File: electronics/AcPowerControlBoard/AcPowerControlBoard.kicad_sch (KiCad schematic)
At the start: 1 part

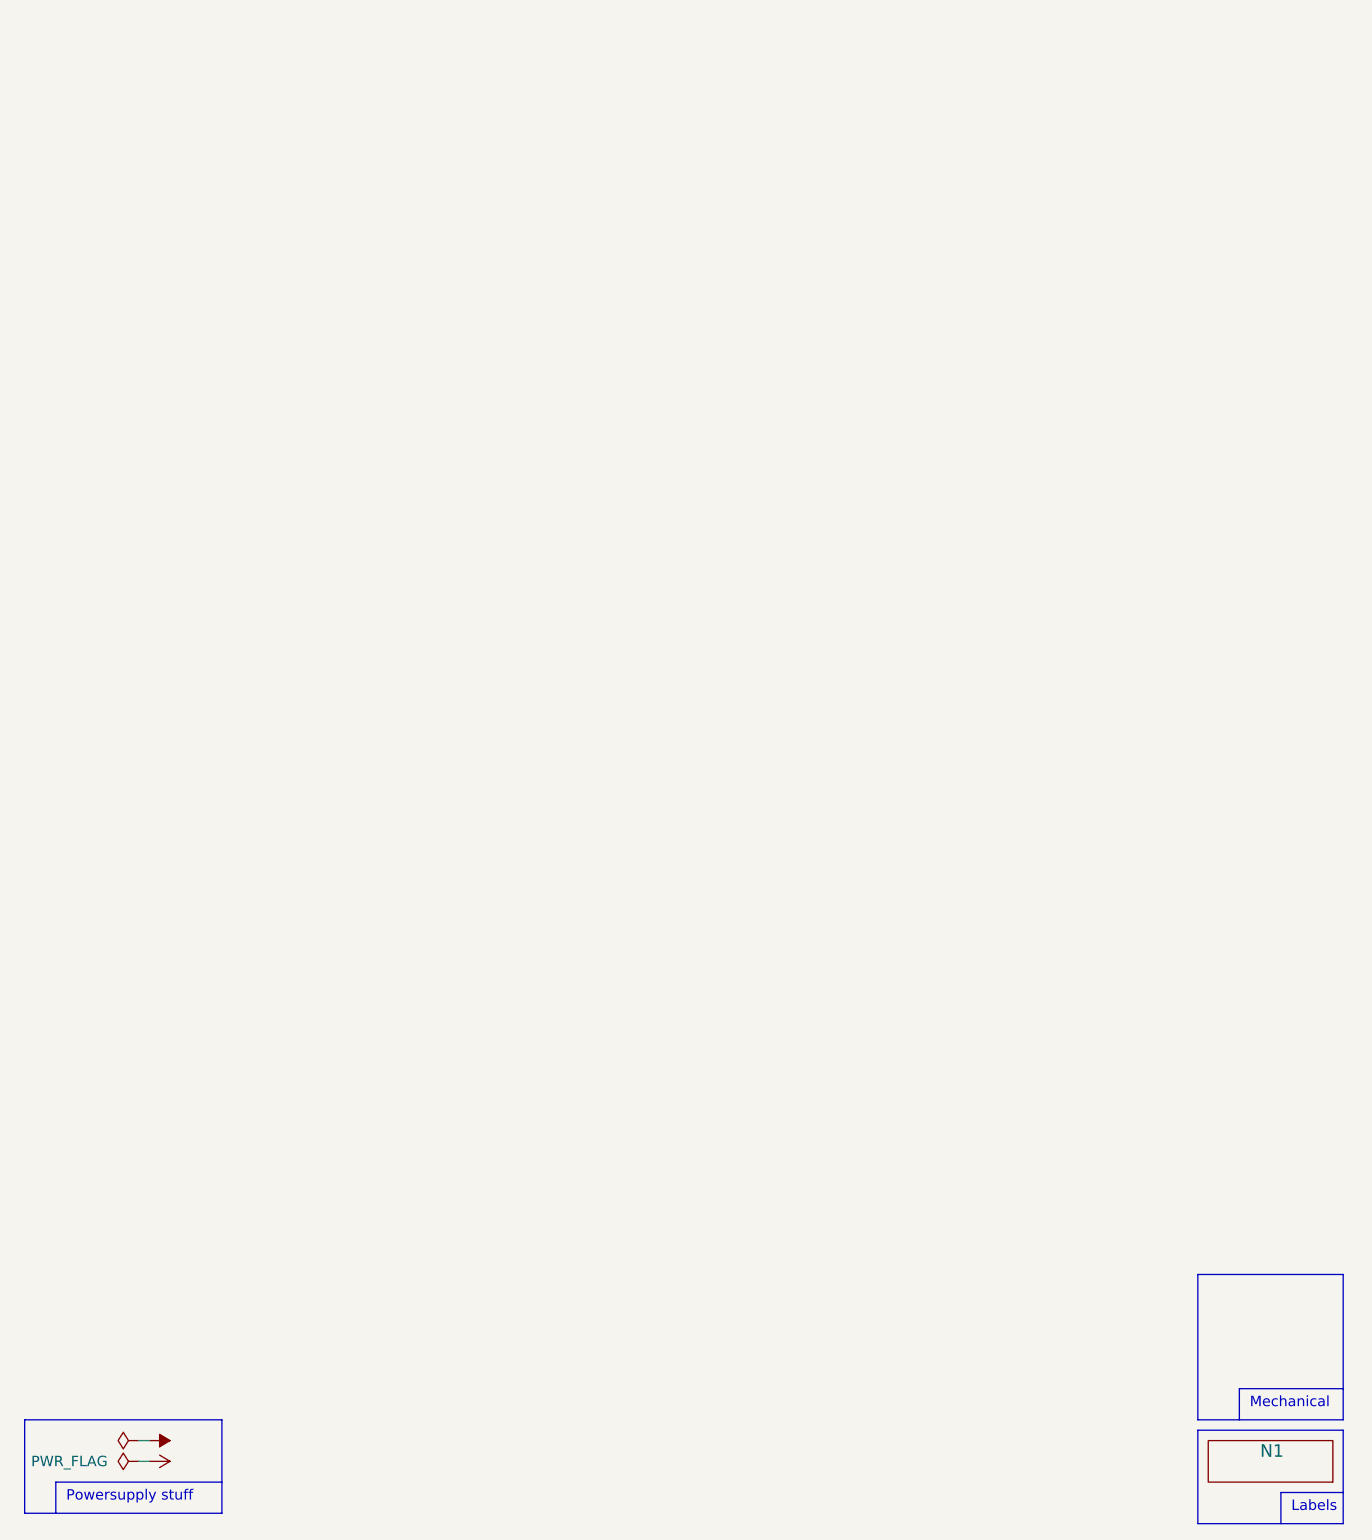
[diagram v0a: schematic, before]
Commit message: added safety relay and rectifier subsystem
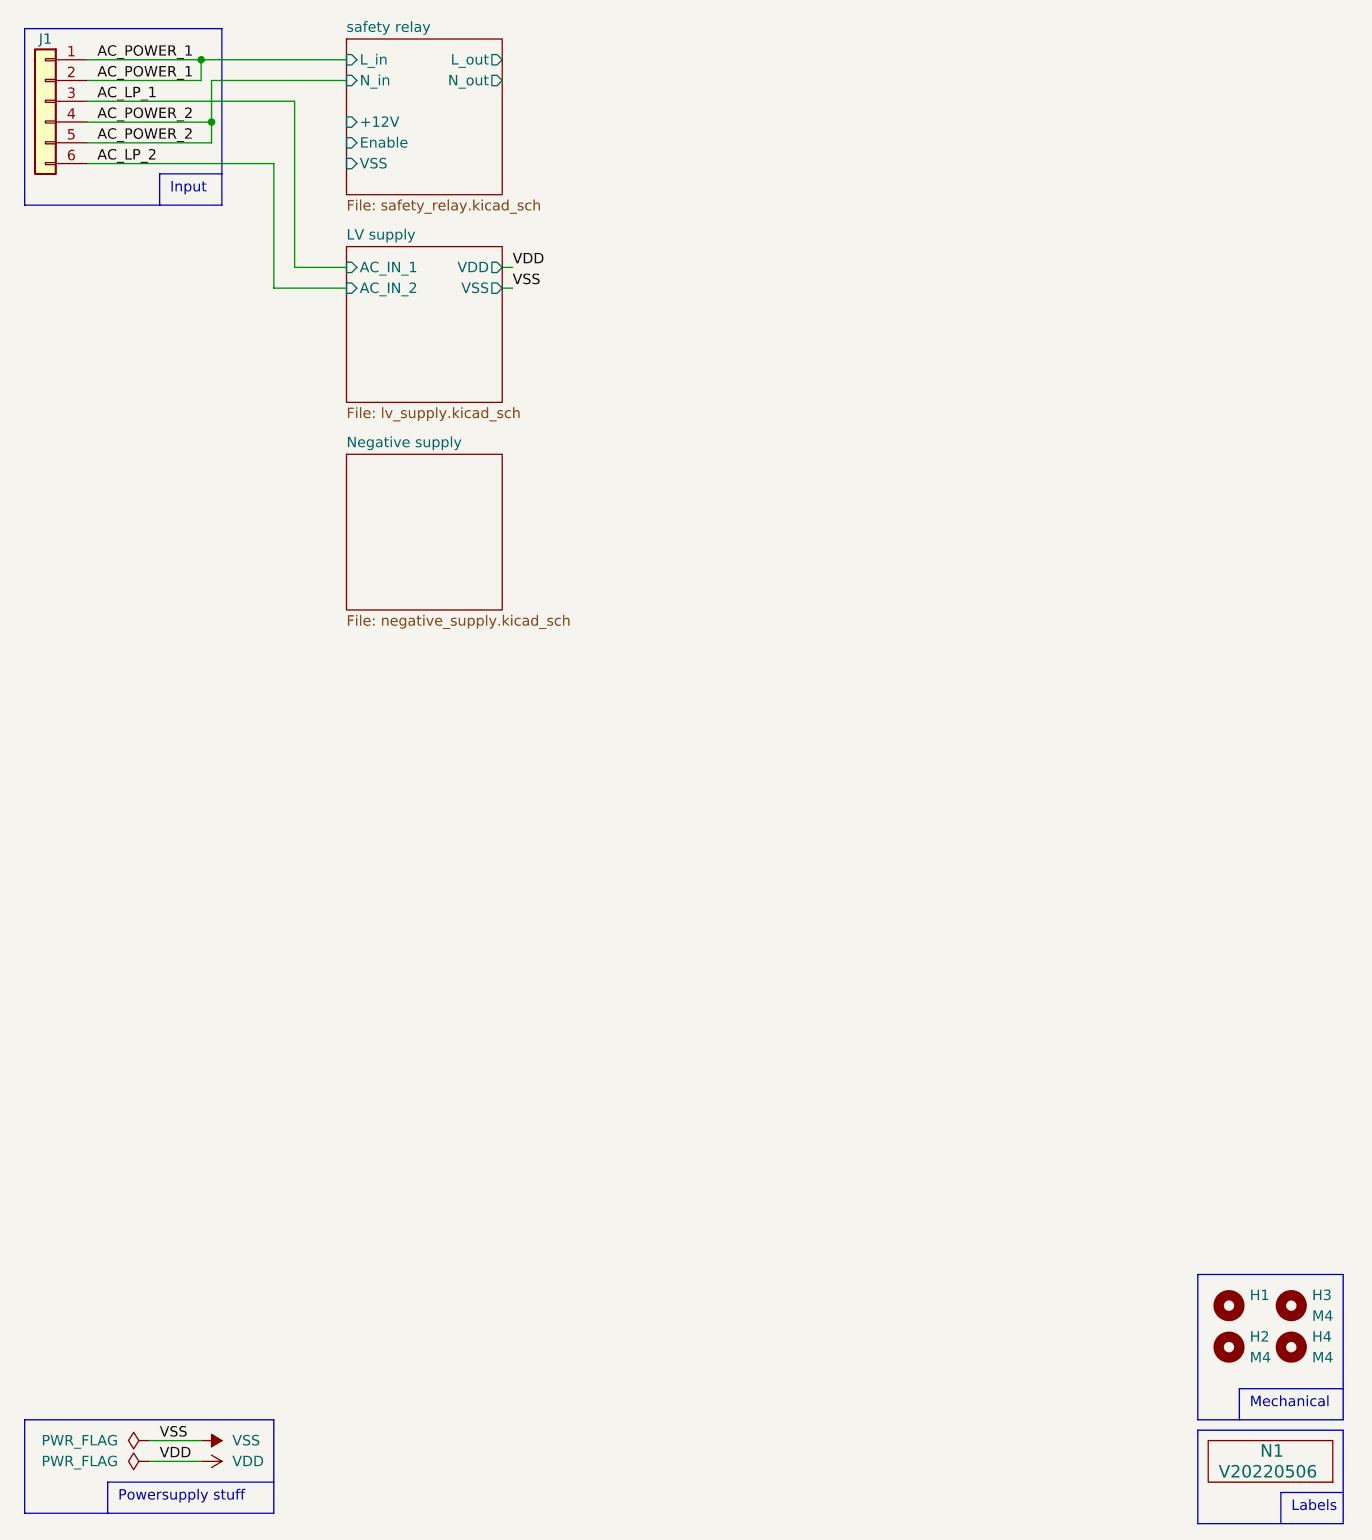
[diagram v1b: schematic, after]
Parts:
- added H1: (no value), symbol Mechanical:MountingHole
- added H2, H3, H4: M4, MountingHole:MountingHole_4.3mm_M4_Pad_Via, symbol Mechanical:MountingHole
- added J1: (no value), symbol Connector_Generic:Conn_01x06
- N1: value (none) -> V20220506; footprint (none) -> SquantorLabels:Label_Generic
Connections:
- new net AC_LP_1: J1.3 (Pin_3)
- new net AC_LP_2: J1.6 (Pin_6)
- new net AC_POWER_1: J1.1 (Pin_1), J1.2 (Pin_2)
- new net AC_POWER_2: J1.4 (Pin_4), J1.5 (Pin_5)
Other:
- added sheet LV supply (lv_supply.kicad_sch)
- added sheet Negative supply (negative_supply.kicad_sch)
- added sheet safety relay (safety_relay.kicad_sch)
- note added: "Input"
